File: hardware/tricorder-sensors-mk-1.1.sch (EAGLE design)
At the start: 21 parts, among them U1 VEML6075, U2 APDS-9250ALT, U3 SI1145QFN-EASIER, U4 TSL2591DFN6

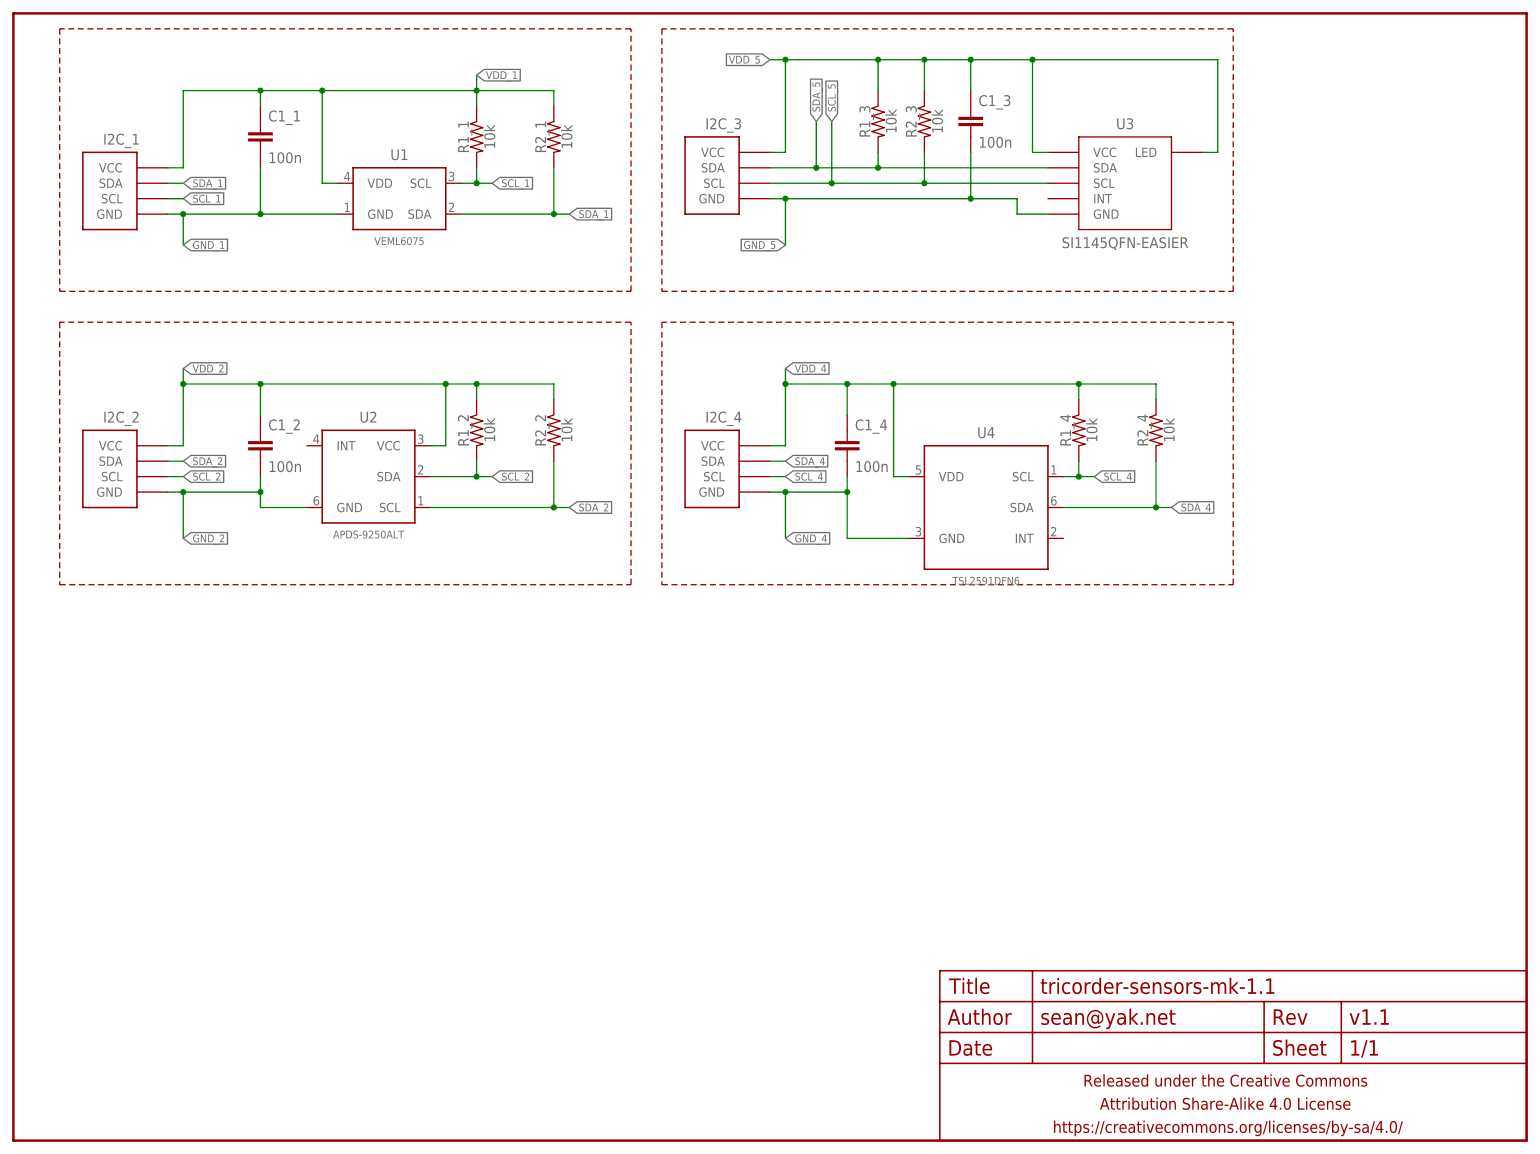
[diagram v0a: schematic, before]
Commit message: relaid out, different set of sensors
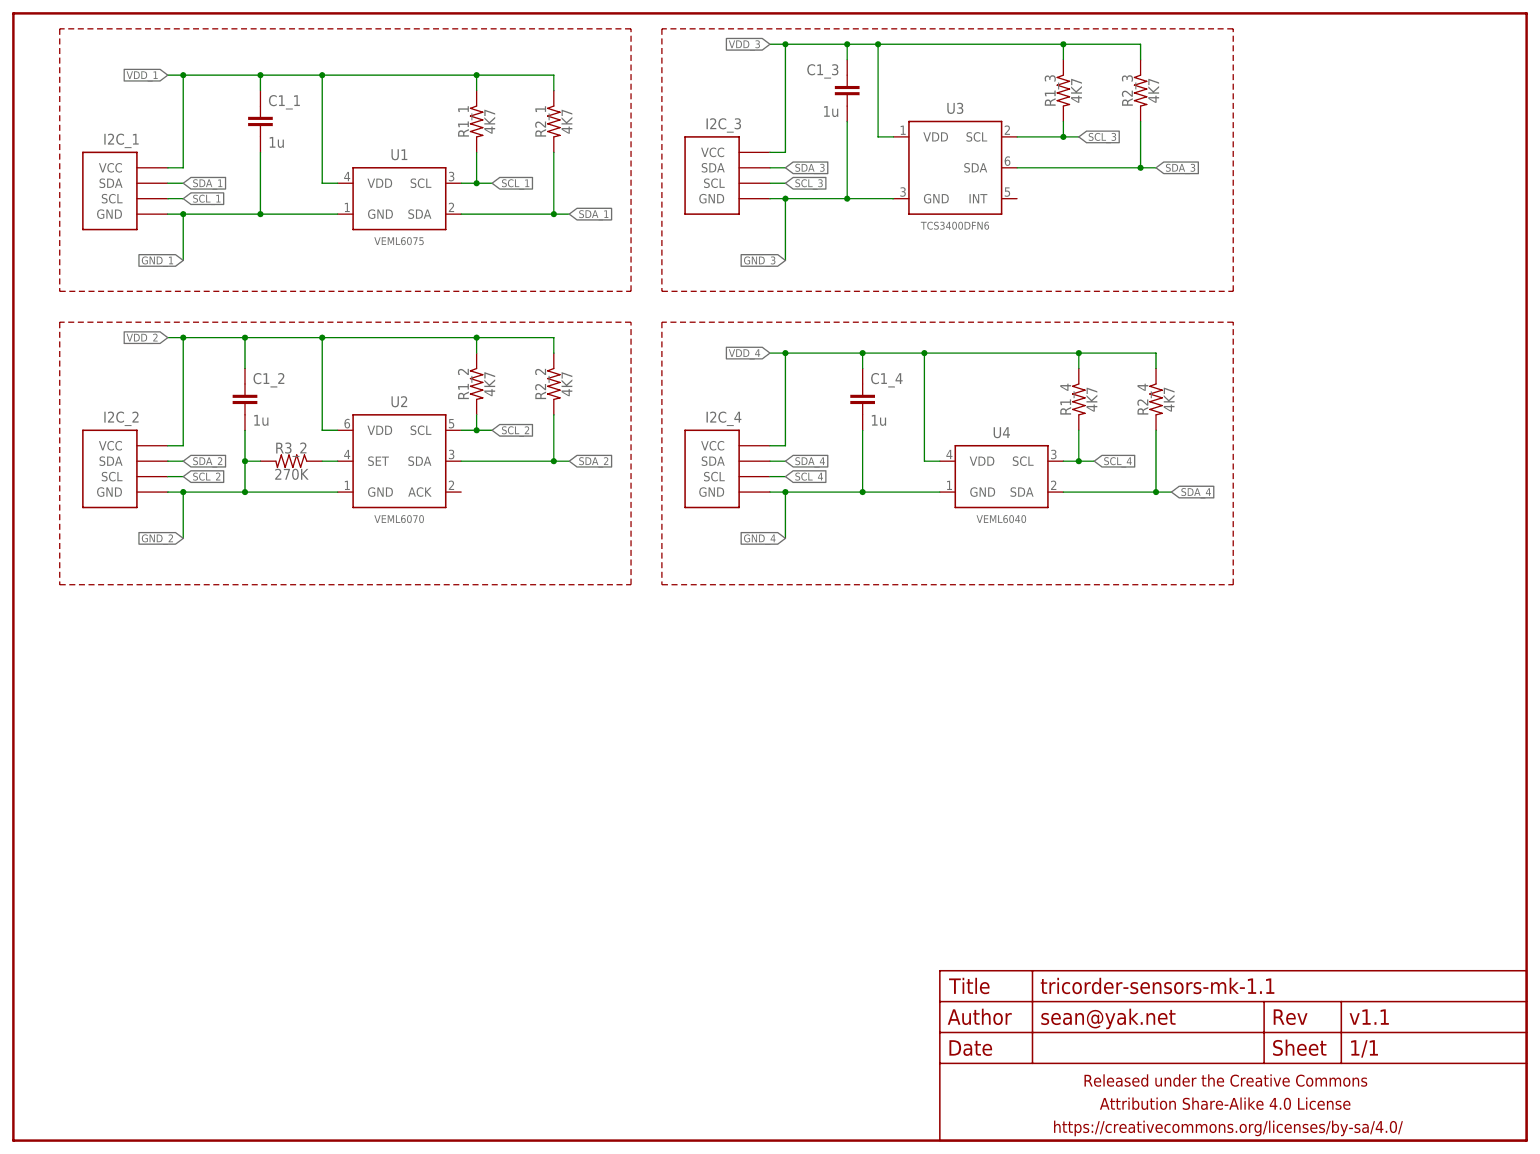
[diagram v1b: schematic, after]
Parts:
- added R3_2: 270K, a_parts:RESISTORR0603
- C1_1, C1_2, C1_3, C1_4: value 100n -> 1u
- R1_1, R1_2, R1_3, R1_4, R2_1, R2_2, R2_3, R2_4: value 10k -> 4K7
- U2: value APDS-9250ALT -> VEML6070; device a_parts:APDS-9250ALT -> a_parts:VEML6070
- U3: value SI1145QFN-EASIER -> TCS3400DFN6; device a_parts:SI1145QFN-EASIER -> a_parts:TCS3400DFN6
- U4: value TSL2591DFN6 -> VEML6040; device a_parts:TSL2591DFN6 -> a_parts:VEML6075
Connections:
- net GND_5 renamed GND_3
- removed net SCL_5: I2C_3.SCL, R2_3.2, U3.SCL
- removed net SDA_5: I2C_3.SDA, R1_3.2, U3.SDA
- removed net VDD_5: C1_3.1, I2C_3.VCC, R1_3.1, R2_3.1, U3.LED, U3.VCC
- new net N$1: R3_2.1, U2.SET
- new net SCL_3: I2C_3.SCL, R1_3.2, U3.SCL
- new net SDA_3: I2C_3.SDA, R2_3.2, U3.SDA
- new net VDD_3: C1_3.1, I2C_3.VCC, R1_3.1, R2_3.1, U3.VDD
- net GND_2: now also R3_2.2
- net SCL_2: now also U2.SCL; no longer U2.SDA
- net SDA_2: now also U2.SDA; no longer U2.SCL
- net VDD_2: now also U2.VDD; no longer U2.VCC
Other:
- moved on the sheet: C1_1, C1_2, C1_3, C1_4, R1_1, R1_2, R1_3, R1_4, R2_1, R2_2, R2_3, R2_4
